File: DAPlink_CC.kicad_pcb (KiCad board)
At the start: 6 copper layers, 33 x 12.5 mm, 89 parts, among them J1 USB_TypeC-24, J2 Conn_01x04, J3 USB_TypeC-24, J4 Conn_01x02, J5 Conn_01x02, J6 Conn_01x04, Q1 YJL2101W, Q2 TPM7002DFN3, U1 ZD25Q80BNIGR, U10 DIO32220LP10, U11 AW33901FCR, U2 SL2.1S, U3 GD32F350G8U6, U4 LP5240HVF, U5 JW5393FSOTI, U6 HC32L110B6YA, U7 LP5240HVF, U8 DIO32220LP10, U9 DIO32220LP10, X1 12MHz

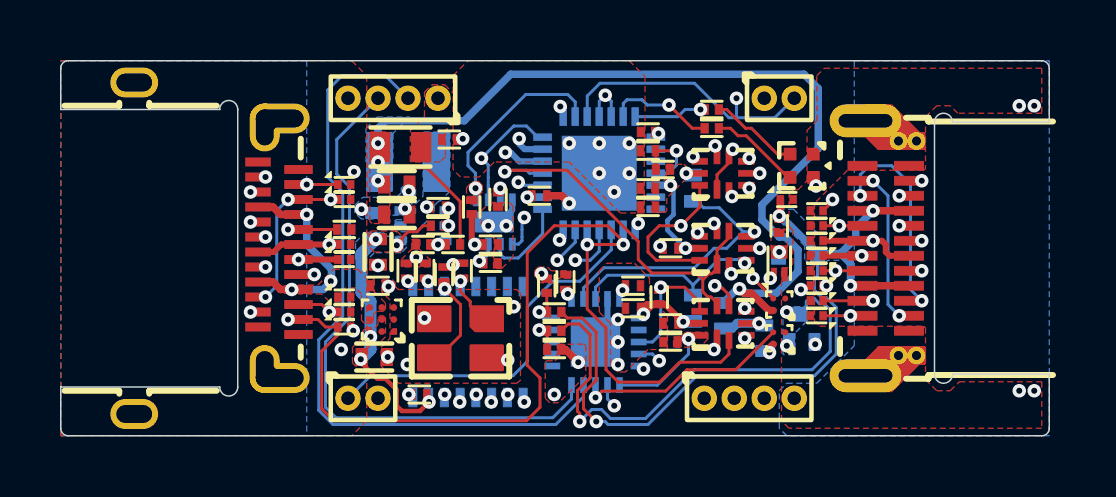
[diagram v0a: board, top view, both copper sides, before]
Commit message: Correction line order of SCF CONN
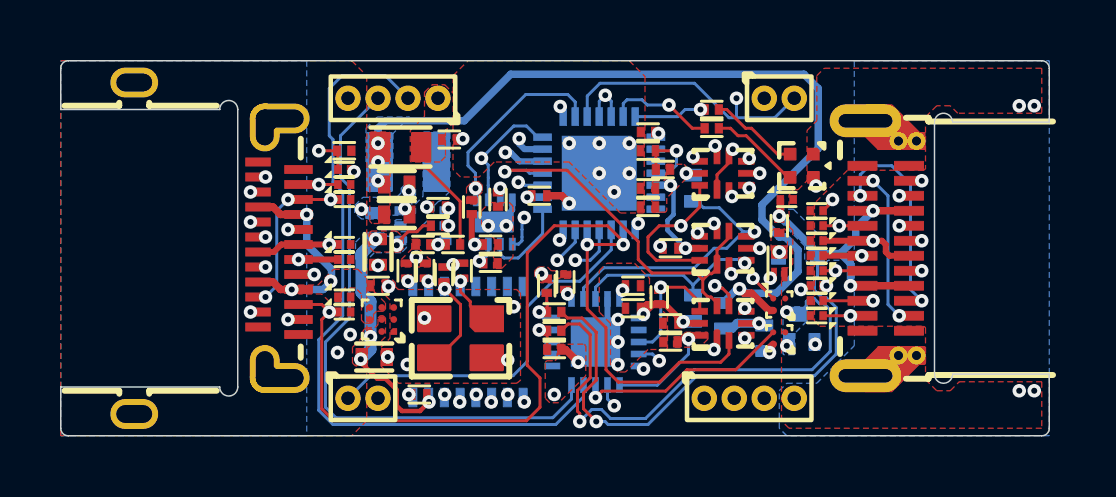
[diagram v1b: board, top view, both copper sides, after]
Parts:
- moved D4 4.75 mm to (101.5, 97.4)
- moved R17 2.62 mm to (101.5, 96.8)
- moved D3 0.50 mm to (101.5, 102.1)
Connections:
- J1 pad A10: /DAP_Tx -> /DAP_Rx
- J1 pad A11: /DAP_Rx -> /DAP_Tx
- J1 pad A5: /DAP_Tx -> /DAP_Rx
- J1 pad B10: /DAP_Tx -> /DAP_Rx
- J1 pad B11: /DAP_Rx -> /DAP_Tx
- J1 pad B5: /DAP_Rx -> /DAP_Tx
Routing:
- net /DAP_Tx: track 27.4 -> 29.9 mm, vias 5 -> 6
- net /DAP_Rx: track 27.4 -> 29.6 mm
- net /DAP_CLK: track 21.9 -> 20.9 mm
